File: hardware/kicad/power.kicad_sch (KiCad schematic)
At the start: 19 parts, among them Q1 DMG3415UQ-7, U10 RT9080-33GJ5, U12 RT9193, U3 TPS22917DBVR, U8 XC6215B332MR-G

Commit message: wip: revision 2
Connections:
- net +3.3V renamed +3V3
- net 2V8_GPS renamed 2V8_GNSS
- net 3V3_GPS renamed 3V3_GNSS
- net VBAT_CELL renamed +BATT_CELL
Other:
- note added: "Sheets Connection"
- note removed: "GNSS 2V8 IO Power"
- note removed: "GNSS 3V3 Main Power"
- moved on the sheet: C20, C21, C23, C24, C26, C45, C46, C47, R3, U12, U3, U8

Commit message: wip: revision 2
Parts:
- added Q2: PMV32UP, Package_TO_SOT_SMD:SOT-23, symbol Device:Q_PMOS_GSD
- added Q7: DMG1012UW, Package_TO_SOT_SMD:SOT-323_SC-70, symbol Device:Q_NMOS_GSD
- added R21, R33: 1M, Resistor_SMD:R_0603_1608Metric, symbol Device:R_Small
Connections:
- net +BATT: now also Q2.2 (S), R21.1
- net GND: now also Q7.2 (S), R33.2
- net +BATT_CELL renamed CELL_BATT
- net 2V8_GNSS renamed GNSS_2V8
- net 3V3_GNSS renamed GNSS_3V3
- net EN_CELL renamed CELL_EN
- net EN_GNSS renamed GNSS_EN
- new net: Q2.1 (G), Q7.3 (D), R21.2
- new net GNSS_VBCKP: Q2.3 (D)
- new net GNSS_VBCKP_EN: Q7.1 (G), R33.1

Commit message: wip: revision 2
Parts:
- removed D2: B5819W, Diode_SMD:D_SOD-123, symbol Device:D_Schottky
- removed D3: ESDBW5V0A1, Capacitor_SMD:C_0402_1005Metric, symbol Device:D_TVS
- removed Q1: DMG3415UQ-7, Package_TO_SOT_SMD:SOT-23, symbol Simulation_SPICE:PMOS
- removed R6: 10k, Resistor_SMD:R_0402_1005Metric, symbol Device:R_Small
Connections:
- net +BATT: now also C5.1, U10.1 (VIN), U10.3 (CE)
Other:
- note added: "GNSS 2V8 IO Power"
- note added: "GNSS 3V3 Main Power"
- note added: "GNSS VBackup Switch"
- note added: "Main 3V3 Power"
- note removed: "Power for MCU, Cellular and GPS"
- moved on the sheet: C20, C21, C23, C24, C26, C4, C45, C46, C47, C5, Q2, Q7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

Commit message: wip: revision 2
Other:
- moved on the sheet: C45, C46, C47, U12

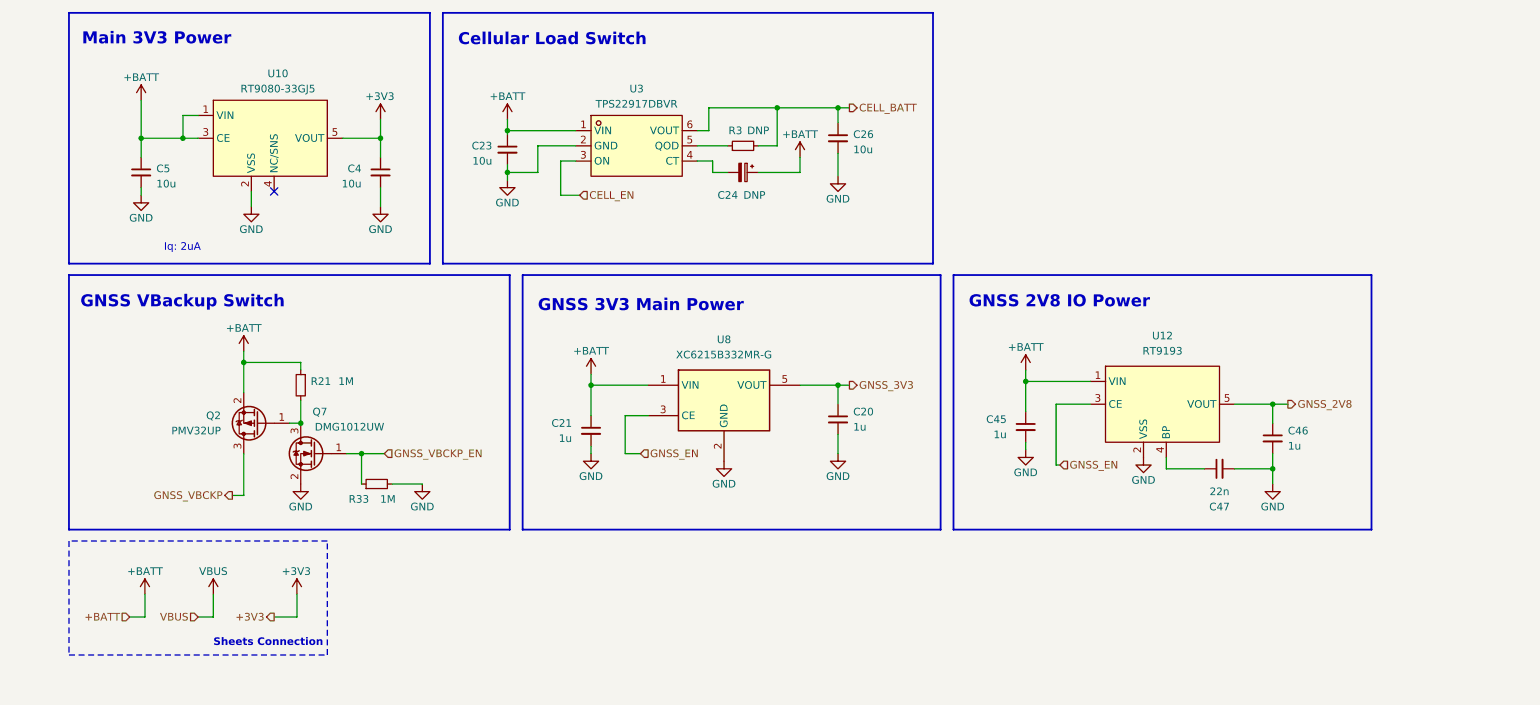
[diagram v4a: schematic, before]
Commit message: clean-up and update antenna
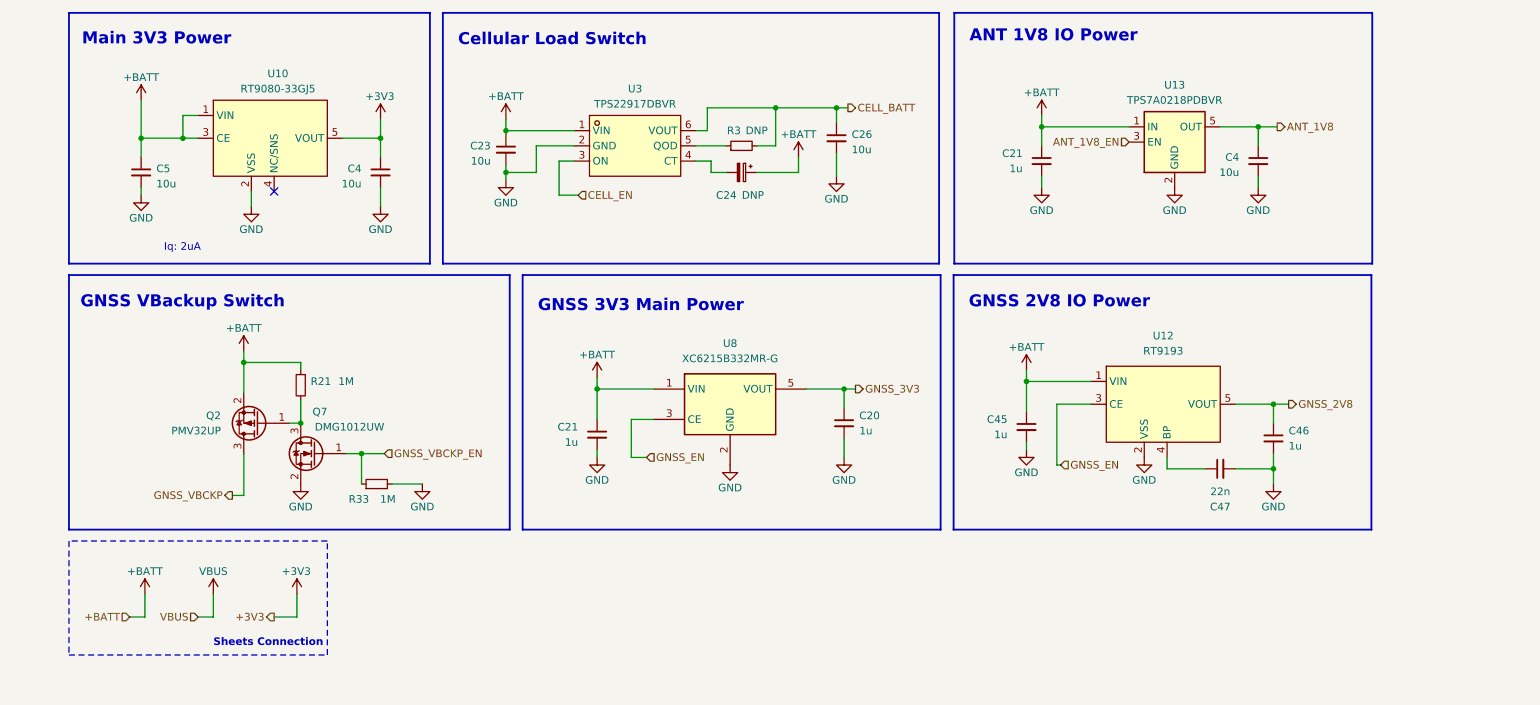
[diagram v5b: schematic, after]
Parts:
- added C21: 1u, Capacitor_SMD:C_0603_1608Metric, symbol Device:C_Small
- added C4: 10u, Capacitor_SMD:C_0603_1608Metric, symbol Device:C_Small
- added U13: TPS7A0218PDBVR, Package_TO_SOT_SMD:SOT-23-5, symbol Regulator_Linear:TPS7A0508PDBV
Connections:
- net +BATT: now also C21.1, U13.1 (IN)
- net GND: now also C21.2, C4.2, U13.2 (GND)
- new net ANT_1V8: C4.1, U13.5 (OUT)
- new net ANT_1V8_EN: U13.3 (EN)
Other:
- note added: "ANT 1V8 IO Power"
- moved on the sheet: C20, C21, U8

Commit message: ignion antenna design
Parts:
- removed C21: 1u, Capacitor_SMD:C_0603_1608Metric, symbol Device:C_Small
- removed C4: 10u, Capacitor_SMD:C_0603_1608Metric, symbol Device:C_Small
- removed U13: TPS7A0218PDBVR, Package_TO_SOT_SMD:SOT-23-5, symbol Regulator_Linear:TPS7A0508PDBV
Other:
- note removed: "ANT 1V8 IO Power"

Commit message: Added Ignion Antenna
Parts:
- removed C20, C21, C45, C46: 1u, Capacitor_SMD:C_0603_1608Metric, symbol Device:C_Small
- removed C47: 22n, Capacitor_SMD:C_0603_1608Metric, symbol Device:C_Small
- removed U12: RT9193, Package_TO_SOT_SMD:SOT-23-5_HandSoldering, symbol bwlc1a:RT9193
- removed U8: XC6215B332MR-G, Package_TO_SOT_SMD:SOT-23-5, symbol Regulator_Linear:XC6210B332MR
- added C21 (x2): 10u, Capacitor_SMD:C_0603_1608Metric, symbol Device:C_Small
- added C21 (x2): 1u, Capacitor_SMD:C_0603_1608Metric, symbol Device:C_Small
- added U10: TPS7A0328DBVR, Package_TO_SOT_SMD:SOT-23-5, symbol Regulator_Linear:TPS7A0508PDBV
- added U12: TPS7A0333DBVR, Package_TO_SOT_SMD:SOT-23-5, symbol Regulator_Linear:TPS7A0508PDBV
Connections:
- net +BATT: now also C21.1, C21.1, U10.1 (IN), U12.1 (IN)
- net GND: now also C21.2, C21.2, C21.2, C21.2, U10.2 (GND), U12.2 (GND)
- net GNSS_2V8: now also C21.1, U10.5 (OUT)
- net GNSS_3V3: now also C21.1, U12.5 (OUT)
- net GNSS_EN: now also U10.3 (EN), U12.3 (EN)
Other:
- note added: "TODO: - does cellular power cap have a specific ESR? (NO, not specify in datasheet) - maybe change GNSS 2V8 with lower Iq https://www.lcsc.com/product-detail/Linear-Voltage-Regulators-LDO_Texas-Instruments-TPS7A0328DBVR_C2862669.html (DONE) - look for lower LDO Iq for GNSS 3V3 (DONE, TPS7A0333DBVR) - consider adding ESD in all schematic"

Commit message: PCB Layout Update
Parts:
- U10: footprint Package_TO_SOT_SMD:SOT-23-5_HandSoldering -> Package_TO_SOT_SMD:SOT-23-5
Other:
- note added: "TODO: - consider adding ESD in all schematic"
- note removed: "TODO: - does cellular power cap have a specific ESR? (NO, not specify in datasheet) - maybe change GNSS 2V8 with lower Iq https://www.lcsc.com/product-detail/Linear-Voltage-Regulators-LDO_Texas-Instruments-TPS7A0328DBVR_C2862669.html (DONE) - look for lower LDO Iq for GNSS 3V3 (DONE, TPS7A0333DBVR) - consider adding ESD in all schematic"
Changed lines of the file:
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@@
     (effects (font (size 2 2) (thickness 0.4) bold) (justify left bottom))
   )
-  (text "TODO:\n- does cellular power cap have a specific ESR? (NO, not specify in datasheet)\n- maybe change GNSS 2V8 with lower Iq https://www.lcsc.com/product-detail/Linear-Voltage-Regulators-LDO_Texas-Instruments-TPS7A0328DBVR_C2862669.html (DONE)\n- look for lower LDO Iq for GNSS 3V3 (DONE, TPS7A0333DBVR)\n- consider adding ESD in all schematic"
-    (at 87.63 133.985 0)
+  (text "TODO:\n- consider adding ESD in all schematic" (at 87.63 128.27 0)
     (effects (font (size 1.27 1.27)) (justify left bottom))
   )
@@
       (effects (font (size 1.27 1.27)))
     )
-    (property "Footprint" "Package_TO_SOT_SMD:SOT-23-5_HandSoldering" (at 76.2 78.105 0)
-      (effects (font (size 1.27 1.27)) hide)
-    )
+    (property "Footprint" "Package_TO_SOT_SMD:SOT-23-5" (at 76.2 78.105 0)
+      (effects (font (size 1.27 1.27)) hide)
+    )
